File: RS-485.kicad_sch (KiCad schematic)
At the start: 9 parts, among them IC1 MAX485ESA+T

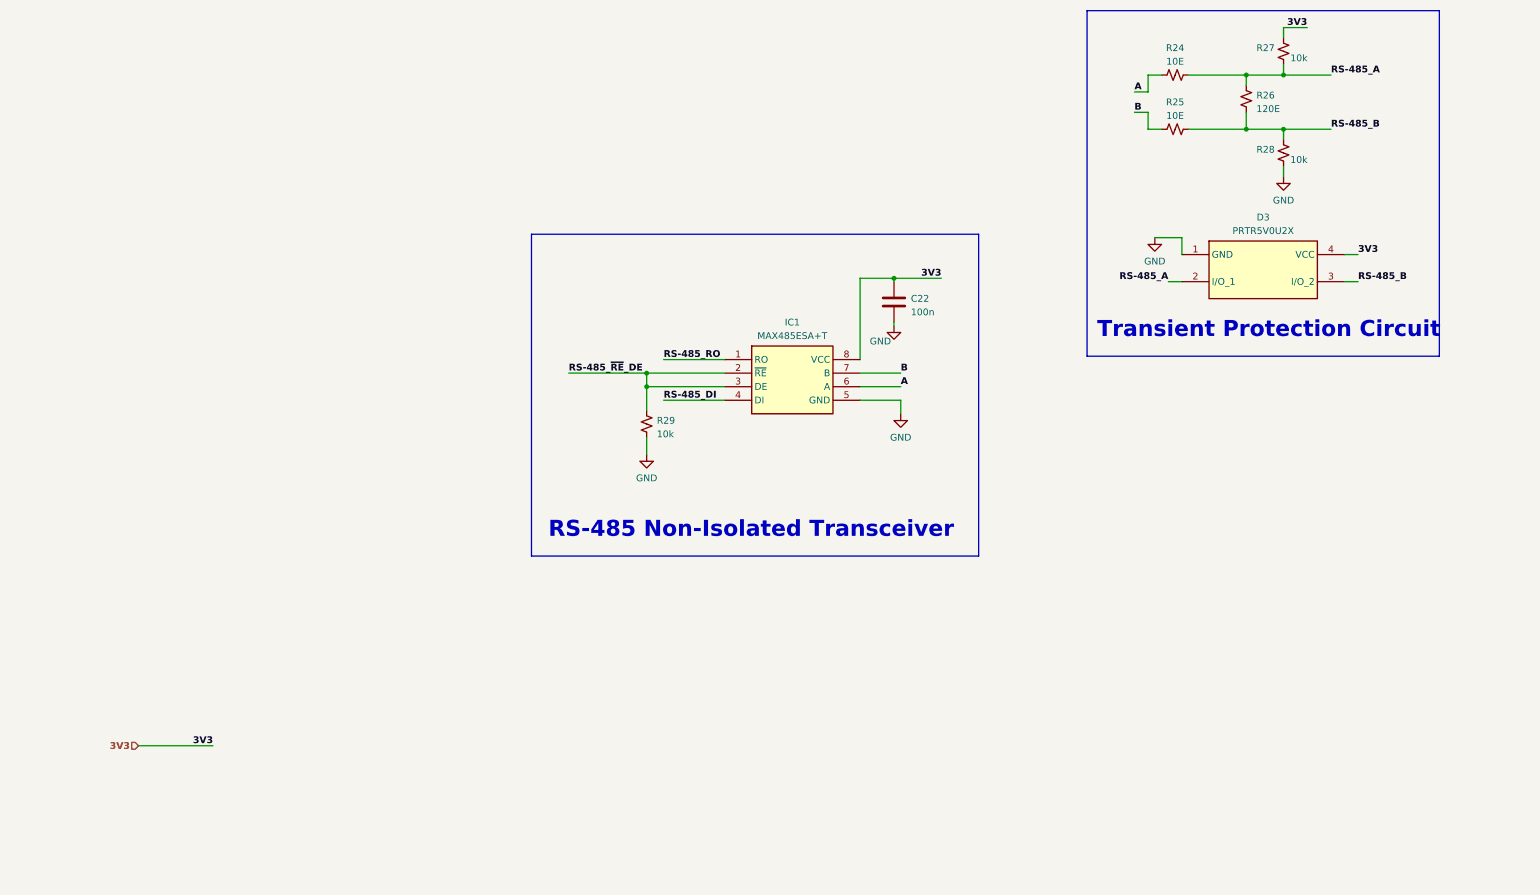
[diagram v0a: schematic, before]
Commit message: Completed RS-485 connections
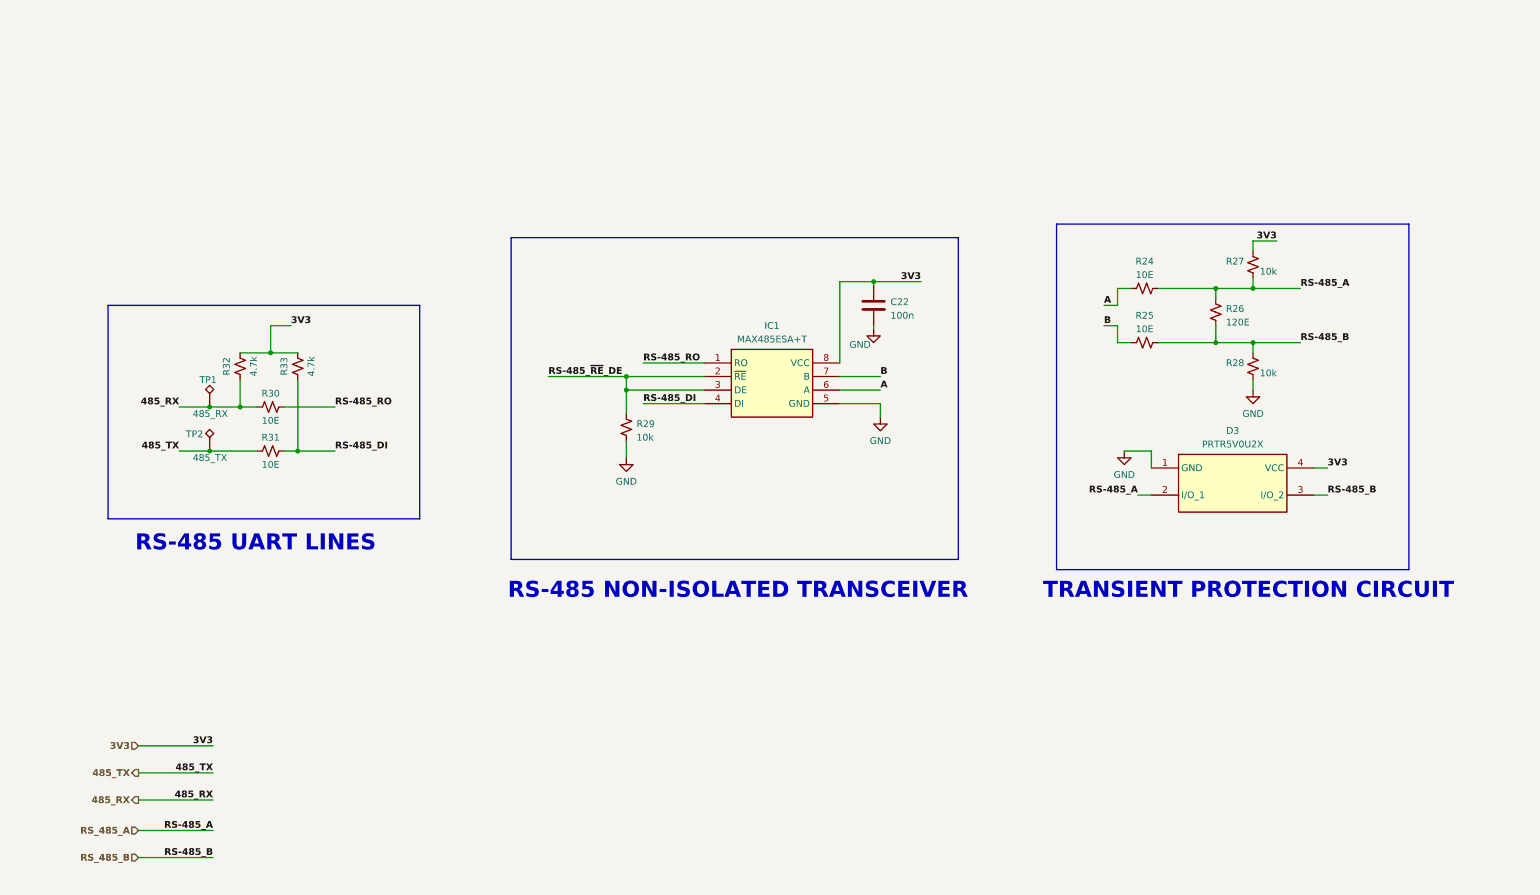
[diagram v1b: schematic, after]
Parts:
- added R30, R31: 10E, symbol ESP32-S3_DB:R_Small_US
- added R32, R33: 4.7k, symbol ESP32-S3_DB:R_Small_US
- added TP1: 485_RX, symbol ESP32-S3_DB:TestPoint_Alt
- added TP2: 485_TX, symbol ESP32-S3_DB:TestPoint_Alt
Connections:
- net 3V3: now also R32.2, R33.2
- net RS-485_DI: now also R31.2, R33.1
- net RS-485_RO: now also R30.2
- net RS-485_A renamed RS_485_A
- net RS-485_B renamed RS_485_B
- new net 485_RX: R30.1, R32.1, TP1.1
- new net 485_TX: R31.1, TP2.1
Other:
- note added: "RS-485 NON-ISOLATED TRANSCEIVER"
- note added: "RS-485 UART LINES"
- note added: "TRANSIENT PROTECTION CIRCUIT"
- note removed: "RS-485 Non-Isolated Transceiver"
- note removed: "Transient Protection Circuit"
- moved on the sheet: C22, D3, IC1, R24, R25, R26, R27, R28, R29

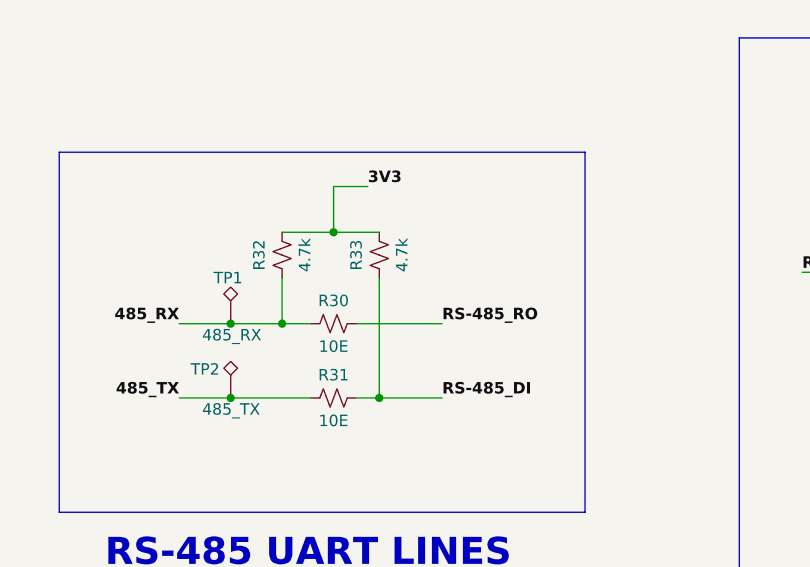
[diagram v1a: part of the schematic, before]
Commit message: Added CAN Transceiver
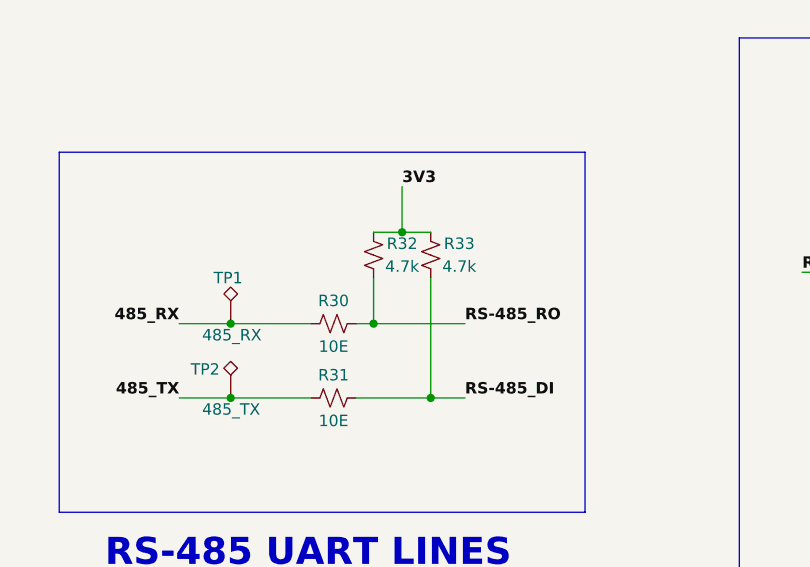
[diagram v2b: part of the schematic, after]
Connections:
- net 485_RX: no longer R32.1
- net RS-485_RO: now also R32.1
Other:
- moved on the sheet: R32, R33
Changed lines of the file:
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@@
   (junction (at 242.57 80.01) (diameter 0) (color 0 0 0 0)
   )
+  (junction (at 69.215 110.49) (diameter 0) (color 0 0 0 0)
+  )
   (junction (at 242.57 90.17) (diameter 0) (color 0 0 0 0)
   )
+  (junction (at 66.04 92.075) (diameter 0) (color 0 0 0 0)
+  )
   (junction (at 235.585 90.17) (diameter 0) (color 0 0 0 0)
   )
   (junction (at 171.45 78.74) (diameter 0) (color 0 0 0 0)
   )
-  (junction (at 58.42 92.075) (diameter 0) (color 0 0 0 0)
-  )
   (junction (at 125.095 99.06) (diameter 0) (color 0 0 0 0)
   )
   (junction (at 46.99 110.49) (diameter 0) (color 0 0 0 0)
   )
-  (junction (at 63.5 110.49) (diameter 0) (color 0 0 0 0)
+  (junction (at 62.865 102.235) (diameter 0) (color 0 0 0 0)
   )
   (junction (at 46.99 102.235) (diameter 0) (color 0 0 0 0)
   )
-  (junction (at 52.705 102.235) (diameter 0) (color 0 0 0 0)
-  )
   (junction (at 125.095 96.52) (diameter 0) (color 0 0 0 0)
   )
@@
     (stroke (width 0) (type default))
   )
-  (wire (pts (xy 58.42 92.075) (xy 63.5 92.075))
-    (stroke (width 0) (type default))
-  )
   (wire (pts (xy 171.45 78.74) (xy 171.45 79.375))
     (stroke (width 0) (type default))
@@
     (stroke (width 0) (type default))
   )
-  (wire (pts (xy 62.23 86.995) (xy 58.42 86.995))
-    (stroke (width 0) (type default))
-  )
   (bus (pts (xy 86.36 123.19) (xy 27.94 123.19))
     (stroke (width 1) (type default) (color 72 72 72 1))
   )
+  (wire (pts (xy 66.04 92.075) (xy 62.865 92.075))
+    (stroke (width 0) (type default))
+  )
   (bus (pts (xy 205.74 132.715) (xy 271.78 132.715))
     (stroke (width 1) (type default) (color 72 72 72 1))
   )
-  (wire (pts (xy 63.5 97.155) (xy 63.5 110.49))
-    (stroke (width 0) (type default))
-  )
   (wire (pts (xy 214.63 83.185) (xy 217.17 83.185))
     (stroke (width 0) (type default))
@@
     (stroke (width 0) (type default))
   )
-  (wire (pts (xy 63.5 110.49) (xy 60.96 110.49))
+  (wire (pts (xy 60.96 110.49) (xy 69.215 110.49))
     (stroke (width 0) (type default))
   )
@@
     (stroke (width 0) (type default))
   )
+  (wire (pts (xy 69.215 97.155) (xy 69.215 110.49))
+    (stroke (width 0) (type default))
+  )
   (bus (pts (xy 187.325 130.81) (xy 103.505 130.81))
     (stroke (width 1) (type default) (color 72 72 72 1))
@@
     (stroke (width 0) (type default))
   )
-  (wire (pts (xy 58.42 86.995) (xy 58.42 92.075))
+  (wire (pts (xy 66.04 86.995) (xy 66.04 92.075))
     (stroke (width 0) (type default))
   )
@@
     (stroke (width 0) (type default))
   )
-  (wire (pts (xy 52.705 102.235) (xy 55.88 102.235))
+  (wire (pts (xy 46.99 102.235) (xy 55.88 102.235))
     (stroke (width 0) (type default))
   )
@@
     (stroke (width 1) (type default) (color 72 72 72 1))
   )
-  (wire (pts (xy 70.485 102.235) (xy 60.96 102.235))
+  (wire (pts (xy 66.04 92.075) (xy 69.215 92.075))
+    (stroke (width 0) (type default))
+  )
+  (wire (pts (xy 73.025 102.235) (xy 62.865 102.235))
     (stroke (width 0) (type default))
   )
@@
     (stroke (width 0) (type default))
   )
-  (wire (pts (xy 52.705 97.155) (xy 52.705 102.235))
-    (stroke (width 0) (type default))
-  )
   (wire (pts (xy 217.17 83.185) (xy 217.17 80.01))
     (stroke (width 0) (type default))
@@
     (stroke (width 1) (type default) (color 72 72 72 1))
   )
+  (wire (pts (xy 62.865 97.155) (xy 62.865 102.235))
+    (stroke (width 0) (type default))
+  )
   (bus (pts (xy 187.325 70.485) (xy 187.325 130.81))
     (stroke (width 1) (type default) (color 72 72 72 1))
@@
     (stroke (width 0) (type default))
   )
-  (wire (pts (xy 70.485 110.49) (xy 63.5 110.49))
+  (wire (pts (xy 62.865 102.235) (xy 60.96 102.235))
     (stroke (width 0) (type default))
   )
@@
     (stroke (width 0) (type default))
   )
-  (wire (pts (xy 46.99 102.235) (xy 52.705 102.235))
-    (stroke (width 0) (type default))
-  )
   (wire (pts (xy 125.095 99.06) (xy 139.7 99.06))
     (stroke (width 0) (type default))
@@
     (stroke (width 0) (type default))
   )
+  (wire (pts (xy 69.215 110.49) (xy 73.025 110.49))
+    (stroke (width 0) (type default))
+  )
   (wire (pts (xy 47.625 165.735) (xy 33.655 165.735))
     (stroke (width 0) (type default))
@@
   )
   (wire (pts (xy 256.54 118.745) (xy 254 118.745))
-    (stroke (width 0) (type default))
-  )
-  (wire (pts (xy 52.705 92.075) (xy 58.42 92.075))
     (stroke (width 0) (type default))
   )
@@
     (effects (font (size 1.27 1.27) (thickness 0.254) bold (color 255 0 0 1)) (justify right bottom))
   )
-  (label "RS-485_RO" (at 70.485 102.235 0) (fields_autoplaced)
+  (label "RS-485_RO" (at 73.025 102.235 0) (fields_autoplaced)
     (effects (font (size 1.27 1.27) bold (color 0 0 255 1)) (justify left bottom))
   )
-  (label "RS-485_DI" (at 70.485 110.49 0) (fields_autoplaced)
+  (label "RS-485_DI" (at 73.025 110.49 0) (fields_autoplaced)
     (effects (font (size 1.27 1.27) bold (color 0 0 255 1)) (justify left bottom))
   )
@@
     (effects (font (size 1.27 1.27) bold (color 0 0 255 1)) (justify left bottom))
   )
-  (label "3V3" (at 62.23 86.995 0) (fields_autoplaced)
+  (label "3V3" (at 66.04 86.995 0) (fields_autoplaced)
     (effects (font (size 1.27 1.27) (thickness 0.254) bold (color 255 0 0 1)) (justify left bottom))
   )
@@
     )
   )
-  (symbol (lib_id "ESP32-S3_DB:R_Small_US") (at 63.5 94.615 180) (unit 1)
+  (symbol (lib_id "ESP32-S3_DB:R_Small_US") (at 69.215 94.615 180) (unit 1)
     (in_bom yes) (on_board yes) (dnp no)
-    (property "Reference" "R33" (at 60.96 94.615 90)
-      (effects (font (size 1.27 1.27)))
-    )
-    (property "Value" "4.7k" (at 66.04 94.615 90)
-      (effects (font (size 1.27 1.27)))
-    )
-    (property "Footprint" "" (at 63.5 94.615 0)
-      (effects (font (size 1.27 1.27)) hide)
-    )
-    (property "Datasheet" "~" (at 63.5 94.615 0)
+    (property "Reference" "R33" (at 72.39 93.345 0)
+      (effects (font (size 1.27 1.27)))
+    )
+    (property "Value" "4.7k" (at 72.39 95.885 0)
+      (effects (font (size 1.27 1.27)))
+    )
+    (property "Footprint" "" (at 69.215 94.615 0)
+      (effects (font (size 1.27 1.27)) hide)
+    )
+    (property "Datasheet" "~" (at 69.215 94.615 0)
       (effects (font (size 1.27 1.27)) hide)
     )
@@
     )
   )
-  (symbol (lib_id "ESP32-S3_DB:R_Small_US") (at 52.705 94.615 180) (unit 1)
+  (symbol (lib_id "ESP32-S3_DB:R_Small_US") (at 62.865 94.615 180) (unit 1)
     (in_bom yes) (on_board yes) (dnp no)
-    (property "Reference" "R32" (at 50.165 94.615 90)
-      (effects (font (size 1.27 1.27)))
-    )
-    (property "Value" "4.7k" (at 55.245 94.615 90)
-      (effects (font (size 1.27 1.27)))
-    )
-    (property "Footprint" "" (at 52.705 94.615 0)
-      (effects (font (size 1.27 1.27)) hide)
-    )
-    (property "Datasheet" "~" (at 52.705 94.615 0)
-      (effects (font (size 1.27 1.27)) hide)
-    )
+    (property "Reference" "R32" (at 66.04 93.345 0)
+      (effects (font (size 1.27 1.27)))
+    )
+    (property "Value" "4.7k" (at 66.04 95.885 0)
+      (effects (font (size 1.27 1.27)))
+    )
+    (property "Footprint" "" (at 62.865 94.615 0)
+      (effects (font (size 1.27 1.27)) hide)
+    )
+    (property "Datasheet" "~" (at 62.865 94.615 0)
+      (effects (font (size 1.27 1.27)) hide)
+    )
